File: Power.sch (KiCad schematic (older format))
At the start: 13 parts, among them P1 24 Pin MiniFit JR, SW1 SWITCH_INV

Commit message: Associating The Filter Module
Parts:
- L1, L2, L3: value INDUCTOR -> CM322522-220KL; MFG Name (none) -> Bournes; MFG Part Number (none) -> CM322522-220KL
- SW1: value SWITCH_INV -> Power Switch; MFG Name (none) -> C&K Components; MFG Part Number (none) -> OS102011MA1QN1
- TH1, TH2, TH3, TH4: value THERMISTOR -> MINISMDC050F-2; MFG Name (none) -> TE Connectivity; MFG Part Number (none) -> MINISMDC050F-2
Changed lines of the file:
@@
-EESchema Schematic File Version 2  date 10/13/2013 8:46:30 PM
+EESchema Schematic File Version 2  date 10/13/2013 11:35:13 PM
 LIBS:power
 LIBS:device
@@
 P 4100 3100
 F 0 "SW1" H 3900 3250 50  0000 C CNN
-F 1 "SWITCH_INV" H 3950 2950 50  0000 C CNN
+F 1 "Power Switch" H 3950 2950 50  0000 C CNN
 F 2 "~" H 4100 3100 60  0000 C CNN
 F 3 "~" H 4100 3100 60  0000 C CNN
+F 4 "C&K Components" H 4100 3100 60  0001 C CNN "MFG Name"
+F 5 "OS102011MA1QN1" H 4100 3100 60  0001 C CNN "MFG Part Number"
 	1    4100 3100
 	1    0    0    -1
@@
 $EndComp
 $Comp
-L INDUCTOR L3
-U 1 1 523E0C8A
-P 8650 2450
-F 0 "L3" V 8600 2450 40  0000 C CNN
-F 1 "INDUCTOR" V 8750 2450 40  0000 C CNN
-F 2 "~" H 8650 2450 60  0000 C CNN
-F 3 "~" H 8650 2450 60  0000 C CNN
-	1    8650 2450
-	0    -1   -1   0
-$EndComp
-$Comp
-L INDUCTOR L2
-U 1 1 523E0C97
-P 8600 3650
-F 0 "L2" V 8550 3650 40  0000 C CNN
-F 1 "INDUCTOR" V 8700 3650 40  0000 C CNN
-F 2 "~" H 8600 3650 60  0000 C CNN
-F 3 "~" H 8600 3650 60  0000 C CNN
-	1    8600 3650
-	0    1    1    0
-$EndComp
-$Comp
 L C C3
 U 1 1 523E0C9F
@@
 P 3900 1500
 F 0 "TH1" V 4000 1550 50  0000 C CNN
-F 1 "THERMISTOR" V 3800 1500 50  0000 C CNN
+F 1 "MINISMDC050F-2" V 3800 1500 50  0000 C CNN
 F 2 "~" H 3900 1500 60  0000 C CNN
 F 3 "~" H 3900 1500 60  0000 C CNN
+F 4 "TE Connectivity" H 3900 1500 60  0001 C CNN "MFG Name"
+F 5 "MINISMDC050F-2" H 3900 1500 60  0001 C CNN "MFG Part Number"
 	1    3900 1500
-	0    -1   -1   0
-$EndComp
-$Comp
-L THERMISTOR TH2
-U 1 1 524396A2
-P 4500 1700
-F 0 "TH2" V 4600 1750 50  0000 C CNN
-F 1 "THERMISTOR" V 4400 1700 50  0000 C CNN
-F 2 "~" H 4500 1700 60  0000 C CNN
-F 3 "~" H 4500 1700 60  0000 C CNN
-	1    4500 1700
-	0    -1   -1   0
-$EndComp
-$Comp
-L THERMISTOR TH3
-U 1 1 524396A8
-P 5050 1900
-F 0 "TH3" V 5150 1950 50  0000 C CNN
-F 1 "THERMISTOR" V 4950 1900 50  0000 C CNN
-F 2 "~" H 5050 1900 60  0000 C CNN
-F 3 "~" H 5050 1900 60  0000 C CNN
-	1    5050 1900
-	0    -1   -1   0
-$EndComp
-$Comp
-L THERMISTOR TH4
-U 1 1 524396AE
-P 5700 2100
-F 0 "TH4" V 5800 2150 50  0000 C CNN
-F 1 "THERMISTOR" V 5600 2100 50  0000 C CNN
-F 2 "~" H 5700 2100 60  0000 C CNN
-F 3 "~" H 5700 2100 60  0000 C CNN
-	1    5700 2100
 	0    -1   -1   0
 $EndComp
@@
 P 8600 900
 F 0 "L1" V 8550 900 40  0000 C CNN
-F 1 "INDUCTOR" V 8700 900 40  0000 C CNN
+F 1 "CM322522-220KL" V 8700 900 40  0000 C CNN
 F 2 "~" H 8600 900 60  0000 C CNN
 F 3 "~" H 8600 900 60  0000 C CNN
+F 4 "Bournes" H 8600 900 60  0001 C CNN "MFG Name"
+F 5 "CM322522-220KL" H 8600 900 60  0001 C CNN "MFG Part Number"
 	1    8600 900
 	0    -1   -1   0
@@
 Wire Wire Line
 	10300 900  10300 650
+$Comp
+L THERMISTOR TH2
+U 1 1 525B6E76
+P 4500 1700
+F 0 "TH2" V 4600 1750 50  0000 C CNN
+F 1 "MINISMDC050F-2" V 4400 1700 50  0000 C CNN
+F 2 "~" H 4500 1700 60  0000 C CNN
+F 3 "~" H 4500 1700 60  0000 C CNN
+F 4 "TE Connectivity" H 4500 1700 60  0001 C CNN "MFG Name"
+F 5 "MINISMDC050F-2" H 4500 1700 60  0001 C CNN "MFG Part Number"
+	1    4500 1700
+	0    -1   -1   0
+$EndComp
+$Comp
+L THERMISTOR TH3
+U 1 1 525B6E7E
+P 5050 1900
+F 0 "TH3" V 5150 1950 50  0000 C CNN
+F 1 "MINISMDC050F-2" V 4950 1900 50  0000 C CNN
+F 2 "~" H 5050 1900 60  0000 C CNN
+F 3 "~" H 5050 1900 60  0000 C CNN
+F 4 "TE Connectivity" H 5050 1900 60  0001 C CNN "MFG Name"
+F 5 "MINISMDC050F-2" H 5050 1900 60  0001 C CNN "MFG Part Number"
+	1    5050 1900
+	0    -1   -1   0
+$EndComp
+$Comp
+L THERMISTOR TH4
+U 1 1 525B6E86
+P 5700 2100
+F 0 "TH4" V 5800 2150 50  0000 C CNN
+F 1 "MINISMDC050F-2" V 5600 2100 50  0000 C CNN
+F 2 "~" H 5700 2100 60  0000 C CNN
+F 3 "~" H 5700 2100 60  0000 C CNN
+F 4 "TE Connectivity" H 5700 2100 60  0001 C CNN "MFG Name"
+F 5 "MINISMDC050F-2" H 5700 2100 60  0001 C CNN "MFG Part Number"
+	1    5700 2100
+	0    -1   -1   0
+$EndComp
+$Comp
+L INDUCTOR L3
+U 1 1 525B71AA
+P 8650 2450
+F 0 "L3" V 8600 2450 40  0000 C CNN
+F 1 "CM322522-220KL" V 8750 2450 40  0000 C CNN
+F 2 "~" H 8650 2450 60  0000 C CNN
+F 3 "~" H 8650 2450 60  0000 C CNN
+F 4 "Bournes" H 8650 2450 60  0001 C CNN "MFG Name"
+F 5 "CM322522-220KL" H 8650 2450 60  0001 C CNN "MFG Part Number"
+	1    8650 2450
+	0    -1   -1   0
+$EndComp
+$Comp
+L INDUCTOR L2
+U 1 1 525B71B2
+P 8600 3650
+F 0 "L2" V 8550 3650 40  0000 C CNN
+F 1 "CM322522-220KL" V 8700 3650 40  0000 C CNN
+F 2 "~" H 8600 3650 60  0000 C CNN
+F 3 "~" H 8600 3650 60  0000 C CNN
+F 4 "Bournes" H 8600 3650 60  0001 C CNN "MFG Name"
+F 5 "CM322522-220KL" H 8600 3650 60  0001 C CNN "MFG Part Number"
+	1    8600 3650
+	0    1    1    0
+$EndComp
 $EndSCHEMATC

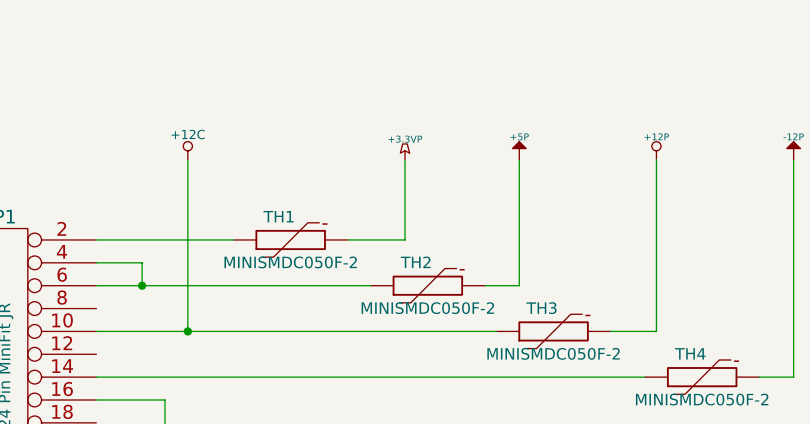
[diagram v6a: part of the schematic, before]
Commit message: Added Ground Planes, Heatsinks, Moved components
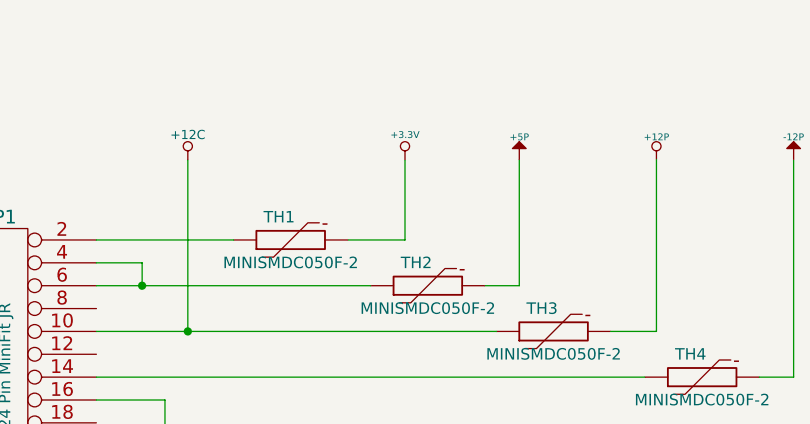
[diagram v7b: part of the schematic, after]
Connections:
- net +3.3VP is gone; now on net +3.3V: TH1.2
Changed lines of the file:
@@
-EESchema Schematic File Version 2  date 10/22/2013 9:09:24 PM
+EESchema Schematic File Version 2  date 10/27/2013 11:25:35 PM
 LIBS:power
 LIBS:device
@@
 $Descr A4 11693 8268
 encoding utf-8
-Sheet 3 9
+Sheet 9 9
 Title ""
-Date "23 oct 2013"
+Date "28 oct 2013"
 Rev ""
 Comp ""
@@
 $EndComp
 $Comp
-L GND #PWR053
+L GND #PWR049
 U 1 1 523DFA76
 P 1400 1850
-F 0 "#PWR053" H 1400 1850 30  0001 C CNN
+F 0 "#PWR049" H 1400 1850 30  0001 C CNN
 F 1 "GND" H 1400 1780 30  0001 C CNN
 F 2 "" H 1400 1850 60  0000 C CNN
@@
 	5500 1900 5500 1150
 $Comp
-L +12P #PWR054
+L +12P #PWR050
 U 1 1 523DFB91
 P 5500 1150
-F 0 "#PWR054" H 5500 1120 30  0001 C CNN
+F 0 "#PWR050" H 5500 1120 30  0001 C CNN
 F 1 "+12P" H 5500 1250 30  0000 C CNN
 F 2 "" H 5500 1150 60  0000 C CNN
@@
 $EndComp
 $Comp
-L -12P #PWR055
+L -12P #PWR051
 U 1 1 523E04D8
 P 6100 1150
-F 0 "#PWR055" H 6100 1280 20  0001 C CNN
+F 0 "#PWR051" H 6100 1280 20  0001 C CNN
 F 1 "-12P" H 6100 1250 30  0000 C CNN
 F 2 "" H 6100 1150 60  0000 C CNN
@@
 	4800 3200 4800 3450
 $Comp
-L GND #PWR056
+L GND #PWR052
 U 1 1 523E08C4
 P 4800 3450
-F 0 "#PWR056" H 4800 3450 30  0001 C CNN
+F 0 "#PWR052" H 4800 3450 30  0001 C CNN
 F 1 "GND" H 4800 3380 30  0001 C CNN
 F 2 "" H 4800 3450 60  0000 C CNN
@@
 	5650 3000 5650 2750
 $Comp
-L +3.3V #PWR057
+L +3.3V #PWR053
 U 1 1 523E0910
 P 5650 2750
-F 0 "#PWR057" H 5650 2710 30  0001 C CNN
+F 0 "#PWR053" H 5650 2710 30  0001 C CNN
 F 1 "+3.3V" H 5650 2860 30  0000 C CNN
 F 2 "" H 5650 2750 60  0000 C CNN
@@
 $EndComp
 $Comp
-L +12P #PWR058
+L +12P #PWR054
 U 1 1 523E0C76
 P 8000 2250
-F 0 "#PWR058" H 8000 2220 30  0001 C CNN
+F 0 "#PWR054" H 8000 2220 30  0001 C CNN
 F 1 "+12P" H 8000 2350 30  0000 C CNN
 F 2 "" H 8000 2250 60  0000 C CNN
@@
 $EndComp
 $Comp
-L -12P #PWR059
+L -12P #PWR055
 U 1 1 523E0C7C
 P 8000 3800
-F 0 "#PWR059" H 8000 3930 20  0001 C CNN
+F 0 "#PWR055" H 8000 3930 20  0001 C CNN
 F 1 "-12P" H 8000 3900 30  0000 C CNN
 F 2 "" H 8000 3800 60  0000 C CNN
@@
 $EndComp
 $Comp
-L GND #PWR060
+L GND #PWR056
 U 1 1 523E0C82
 P 9000 3200
-F 0 "#PWR060" H 9000 3200 30  0001 C CNN
+F 0 "#PWR056" H 9000 3200 30  0001 C CNN
 F 1 "GND" H 9000 3130 30  0001 C CNN
 F 2 "" H 9000 3200 60  0000 C CNN
@@
 Connection ~ 9450 3050
 $Comp
-L -12V #PWR061
+L -12V #PWR057
 U 1 1 523E0DD3
 P 10350 3800
-F 0 "#PWR061" H 10350 3930 20  0001 C CNN
+F 0 "#PWR057" H 10350 3930 20  0001 C CNN
 F 1 "-12V" H 10350 3900 30  0000 C CNN
 F 2 "" H 10350 3800 60  0000 C CNN
@@
 Connection ~ 9450 2450
 $Comp
-L +12V #PWR062
+L +12V #PWR058
 U 1 1 523E0E37
 P 10350 2200
-F 0 "#PWR062" H 10350 2150 20  0001 C CNN
+F 0 "#PWR058" H 10350 2150 20  0001 C CNN
 F 1 "+12V" H 10350 2300 30  0000 C CNN
 F 2 "" H 10350 2200 60  0000 C CNN
@@
 Connection ~ 3450 1900
 $Comp
-L +12C #PWR063
+L +12C #PWR059
 U 1 1 52438F0D
 P 3450 1150
-F 0 "#PWR063" H 3450 1120 30  0001 C CNN
+F 0 "#PWR059" H 3450 1120 30  0001 C CNN
 F 1 "+12C" H 3450 1260 40  0000 C CNN
 F 2 "~" H 3450 1150 60  0000 C CNN
@@
 $EndComp
 $Comp
-L GND #PWR064
+L GND #PWR060
 U 1 1 524502FC
 P 9400 1650
-F 0 "#PWR064" H 9400 1650 30  0001 C CNN
+F 0 "#PWR060" H 9400 1650 30  0001 C CNN
 F 1 "GND" H 9400 1580 30  0001 C CNN
 F 2 "" H 9400 1650 60  0000 C CNN
@@
 $EndComp
 $Comp
-L +3.3VP #PWR065
-U 1 1 52450364
-P 4400 1150
-F 0 "#PWR065" H 4450 1180 20  0001 C CNN
-F 1 "+3.3VP" H 4400 1240 30  0000 C CNN
-F 2 "~" H 4400 1150 60  0000 C CNN
-F 3 "~" H 4400 1150 60  0000 C CNN
-	1    4400 1150
-	1    0    0    -1
-$EndComp
-$Comp
 L +5P #PWR62
 U 1 1 52450371
@@
 $EndComp
 $Comp
-L +5V #PWR066
+L +5V #PWR061
 U 1 1 524503B6
 P 10300 650
-F 0 "#PWR066" H 10300 740 20  0001 C CNN
+F 0 "#PWR061" H 10300 740 20  0001 C CNN
 F 1 "+5V" H 10300 740 30  0000 C CNN
 F 2 "~" H 10300 650 60  0000 C CNN
@@
 	0    1    1    0
 $EndComp
+$Comp
+L +3.3V #PWR062
+U 1 1 526E168C
+P 4400 1150
+F 0 "#PWR062" H 4400 1110 30  0001 C CNN
+F 1 "+3.3V" H 4400 1260 30  0000 C CNN
+F 2 "" H 4400 1150 60  0000 C CNN
+F 3 "" H 4400 1150 60  0000 C CNN
+	1    4400 1150
+	1    0    0    -1
+$EndComp
 $EndSCHEMATC

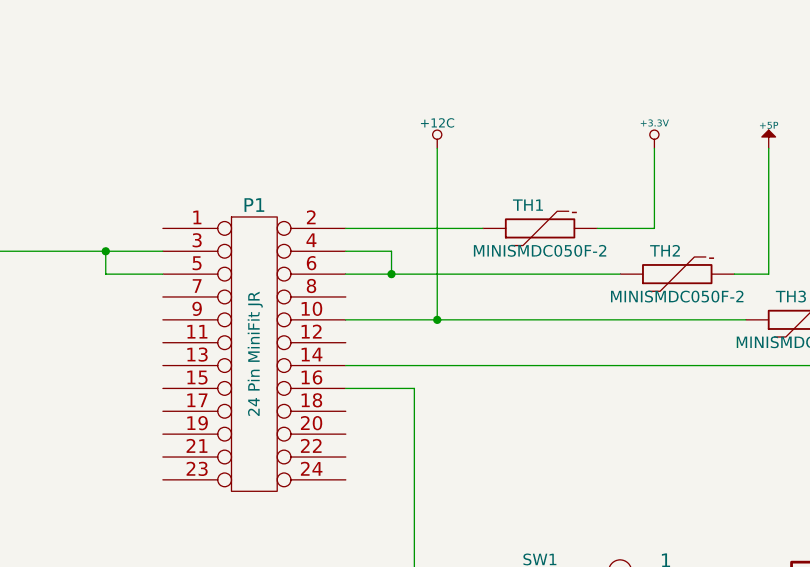
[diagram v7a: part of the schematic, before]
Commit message: More ground plane changes
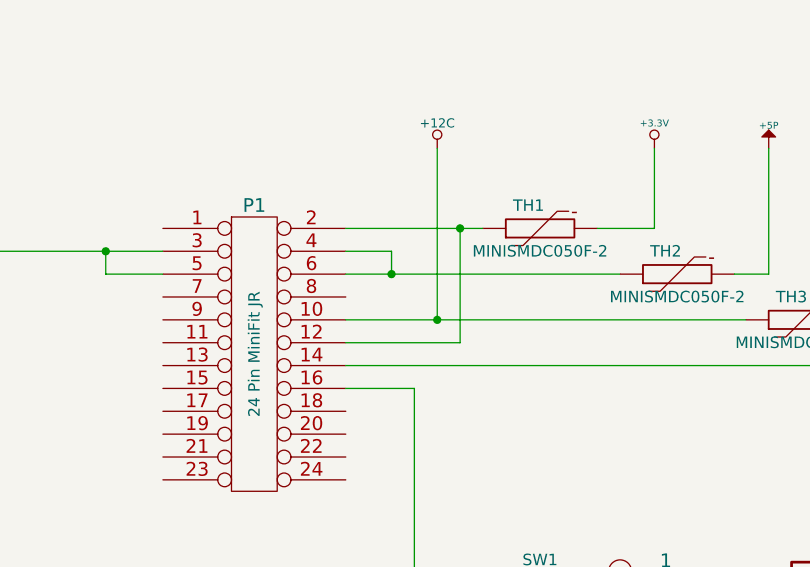
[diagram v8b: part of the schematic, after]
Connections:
- net at P1.12 (P12): now also P1.2 (P2), TH1.1
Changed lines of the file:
@@
-EESchema Schematic File Version 2  date 10/27/2013 11:25:35 PM
+EESchema Schematic File Version 2  date 10/31/2013 9:00:44 PM
 LIBS:power
 LIBS:device
@@
 Sheet 9 9
 Title ""
-Date "28 oct 2013"
+Date "1 nov 2013"
 Rev ""
 Comp ""
@@
 $EndComp
 $Comp
-L GND #PWR049
+L GND #PWR54
 U 1 1 523DFA76
 P 1400 1850
-F 0 "#PWR049" H 1400 1850 30  0001 C CNN
+F 0 "#PWR54" H 1400 1850 30  0001 C CNN
 F 1 "GND" H 1400 1780 30  0001 C CNN
 F 2 "" H 1400 1850 60  0000 C CNN
@@
 	5500 1900 5500 1150
 $Comp
-L +12P #PWR050
+L +12P #PWR59
 U 1 1 523DFB91
 P 5500 1150
-F 0 "#PWR050" H 5500 1120 30  0001 C CNN
+F 0 "#PWR59" H 5500 1120 30  0001 C CNN
 F 1 "+12P" H 5500 1250 30  0000 C CNN
 F 2 "" H 5500 1150 60  0000 C CNN
@@
 $EndComp
 $Comp
-L -12P #PWR051
+L -12P #PWR61
 U 1 1 523E04D8
 P 6100 1150
-F 0 "#PWR051" H 6100 1280 20  0001 C CNN
+F 0 "#PWR61" H 6100 1280 20  0001 C CNN
 F 1 "-12P" H 6100 1250 30  0000 C CNN
 F 2 "" H 6100 1150 60  0000 C CNN
@@
 	4800 3200 4800 3450
 $Comp
-L GND #PWR052
+L GND #PWR57
 U 1 1 523E08C4
 P 4800 3450
-F 0 "#PWR052" H 4800 3450 30  0001 C CNN
+F 0 "#PWR57" H 4800 3450 30  0001 C CNN
 F 1 "GND" H 4800 3380 30  0001 C CNN
 F 2 "" H 4800 3450 60  0000 C CNN
@@
 	5650 3000 5650 2750
 $Comp
-L +3.3V #PWR053
+L +3.3V #PWR60
 U 1 1 523E0910
 P 5650 2750
-F 0 "#PWR053" H 5650 2710 30  0001 C CNN
+F 0 "#PWR60" H 5650 2710 30  0001 C CNN
 F 1 "+3.3V" H 5650 2860 30  0000 C CNN
 F 2 "" H 5650 2750 60  0000 C CNN
@@
 $EndComp
 $Comp
-L +12P #PWR054
+L +12P #PWR63
 U 1 1 523E0C76
 P 8000 2250
-F 0 "#PWR054" H 8000 2220 30  0001 C CNN
+F 0 "#PWR63" H 8000 2220 30  0001 C CNN
 F 1 "+12P" H 8000 2350 30  0000 C CNN
 F 2 "" H 8000 2250 60  0000 C CNN
@@
 $EndComp
 $Comp
-L -12P #PWR055
+L -12P #PWR64
 U 1 1 523E0C7C
 P 8000 3800
-F 0 "#PWR055" H 8000 3930 20  0001 C CNN
+F 0 "#PWR64" H 8000 3930 20  0001 C CNN
 F 1 "-12P" H 8000 3900 30  0000 C CNN
 F 2 "" H 8000 3800 60  0000 C CNN
@@
 $EndComp
 $Comp
-L GND #PWR056
+L GND #PWR65
 U 1 1 523E0C82
 P 9000 3200
-F 0 "#PWR056" H 9000 3200 30  0001 C CNN
+F 0 "#PWR65" H 9000 3200 30  0001 C CNN
 F 1 "GND" H 9000 3130 30  0001 C CNN
 F 2 "" H 9000 3200 60  0000 C CNN
@@
 Connection ~ 9450 3050
 $Comp
-L -12V #PWR057
+L -12V #PWR69
 U 1 1 523E0DD3
 P 10350 3800
-F 0 "#PWR057" H 10350 3930 20  0001 C CNN
+F 0 "#PWR69" H 10350 3930 20  0001 C CNN
 F 1 "-12V" H 10350 3900 30  0000 C CNN
 F 2 "" H 10350 3800 60  0000 C CNN
@@
 Connection ~ 9450 2450
 $Comp
-L +12V #PWR058
+L +12V #PWR68
 U 1 1 523E0E37
 P 10350 2200
-F 0 "#PWR058" H 10350 2150 20  0001 C CNN
+F 0 "#PWR68" H 10350 2150 20  0001 C CNN
 F 1 "+12V" H 10350 2300 30  0000 C CNN
 F 2 "" H 10350 2200 60  0000 C CNN
@@
 Connection ~ 3450 1900
 $Comp
-L +12C #PWR059
+L +12C #PWR55
 U 1 1 52438F0D
 P 3450 1150
-F 0 "#PWR059" H 3450 1120 30  0001 C CNN
+F 0 "#PWR55" H 3450 1120 30  0001 C CNN
 F 1 "+12C" H 3450 1260 40  0000 C CNN
 F 2 "~" H 3450 1150 60  0000 C CNN
@@
 $EndComp
 $Comp
-L GND #PWR060
+L GND #PWR66
 U 1 1 524502FC
 P 9400 1650
-F 0 "#PWR060" H 9400 1650 30  0001 C CNN
+F 0 "#PWR66" H 9400 1650 30  0001 C CNN
 F 1 "GND" H 9400 1580 30  0001 C CNN
 F 2 "" H 9400 1650 60  0000 C CNN
@@
 $EndComp
 $Comp
-L +5V #PWR061
+L +5V #PWR67
 U 1 1 524503B6
 P 10300 650
-F 0 "#PWR061" H 10300 740 20  0001 C CNN
+F 0 "#PWR67" H 10300 740 20  0001 C CNN
 F 1 "+5V" H 10300 740 30  0000 C CNN
 F 2 "~" H 10300 650 60  0000 C CNN
@@
 $EndComp
 $Comp
-L +3.3V #PWR062
+L +3.3V #PWR56
 U 1 1 526E168C
 P 4400 1150
-F 0 "#PWR062" H 4400 1110 30  0001 C CNN
+F 0 "#PWR56" H 4400 1110 30  0001 C CNN
 F 1 "+3.3V" H 4400 1260 30  0000 C CNN
 F 2 "" H 4400 1150 60  0000 C CNN
@@
 	1    0    0    -1
 $EndComp
+Wire Wire Line
+	3050 2000 3550 2000
+Wire Wire Line
+	3550 2000 3550 1500
+Connection ~ 3550 1500
 $EndSCHEMATC
